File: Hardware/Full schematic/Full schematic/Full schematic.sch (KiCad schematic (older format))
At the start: 23 parts, among them J1 Conn_01x04_Male, J2 Conn_01x02_Male, U1 74LVC2T45DC, U2 74LVC2T45DC, U3 AD9835, X1 50MHz

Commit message: Fixed power control bug
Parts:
- added C10: 0.1uF, symbol Device:C
- added C11, C13: 47pF, symbol Device:C
- added C12: 56pF, symbol Device:C
- added L1, L4: 3.3uH, symbol Device:L
- added L2, L3: 4.7uH, symbol Device:L
- gave numbers to parts that had none: 6
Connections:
- net GND: now also C11.2, C12.2, C13.2
- net at R1.1, U3.14 (IOUT): now also C10.2; no longer J2.2 (Pin_2)
- new net: C10.1, L1.1
- new net: C11.1, L1.2, L2.1
- new net: J2.2 (Pin_2), L4.2
- new net: C12.1, L2.2, L3.1
- new net: C13.1, L3.2, L4.1
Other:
- note added: "Peak to peak:\n3.50MHz - ?\n3.65MHz - ?\n18.00MHz - ?\n18.25MHz - ?"
- moved on the sheet: J2
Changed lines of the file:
@@
 Wire Wire Line
 	6500 3300 6300 3300
-$Comp
-L Connector:Conn_01x02_Male J2
-U 1 1 5FE33216
-P 7050 3400
-F 0 "J2" H 7112 3444 50  0000 L CNN
-F 1 "Conn_01x02_Male" V 7203 3444 50  0000 L CNN
-F 2 "" H 7050 3400 50  0001 C CNN
-F 3 "~" H 7050 3400 50  0001 C CNN
-	1    7050 3400
-	-1   0    0    1
-$EndComp
-Wire Wire Line
-	6850 3300 6500 3300
-Connection ~ 6500 3300
-$Comp
-L power:GND #PWR026
-U 1 1 5FE3B38F
-P 6800 3450
-F 0 "#PWR026" H 6800 3200 50  0001 C CNN
-F 1 "GND" H 6805 3277 50  0000 C CNN
-F 2 "" H 6800 3450 50  0001 C CNN
-F 3 "" H 6800 3450 50  0001 C CNN
-	1    6800 3450
-	1    0    0    -1
-$EndComp
-Wire Wire Line
-	6800 3450 6800 3400
-Wire Wire Line
-	6800 3400 6850 3400
-Text Notes 7100 3350 0    50   ~ 0
-Clock out
-$Comp
-L Device:R R?
+Wire Wire Line
+	10450 3450 10450 3400
+$Comp
+L Device:R R6
 U 1 1 5FDFBB2B
 P 3800 1700
-F 0 "R?" V 3593 1700 50  0000 C CNN
+F 0 "R6" V 3593 1700 50  0000 C CNN
 F 1 "100" V 3684 1700 50  0000 C CNN
 F 2 "" V 3730 1700 50  0001 C CNN
@@
 $EndComp
 $Comp
-L Device:R R?
+L Device:R R7
 U 1 1 5FDFCB33
 P 4000 1900
-F 0 "R?" V 3793 1900 50  0000 C CNN
+F 0 "R7" V 3793 1900 50  0000 C CNN
 F 1 "100" V 3884 1900 50  0000 C CNN
 F 2 "" V 3930 1900 50  0001 C CNN
@@
 $EndComp
 $Comp
-L Device:R R?
+L Device:R R8
 U 1 1 5FDFD6DE
 P 4100 2500
-F 0 "R?" V 3893 2500 50  0000 C CNN
+F 0 "R8" V 3893 2500 50  0000 C CNN
 F 1 "100" V 3984 2500 50  0000 C CNN
 F 2 "" V 4030 2500 50  0001 C CNN
@@
 	4250 2500 5200 2500
 $Comp
-L Device:R R?
+L Device:R R3
 U 1 1 5FE1FFE2
 P 1950 1700
-F 0 "R?" V 1743 1700 50  0000 C CNN
+F 0 "R3" V 1743 1700 50  0000 C CNN
 F 1 "100" V 1950 1700 50  0000 C CNN
 F 2 "" V 1880 1700 50  0001 C CNN
@@
 $EndComp
 $Comp
-L Device:R R?
+L Device:R R4
 U 1 1 5FE20C21
 P 1950 1800
-F 0 "R?" V 1743 1800 50  0000 C CNN
+F 0 "R4" V 1743 1800 50  0000 C CNN
 F 1 "100" V 1950 1800 50  0000 C CNN
 F 2 "" V 1880 1800 50  0001 C CNN
@@
 $EndComp
 $Comp
-L Device:R R?
+L Device:R R5
 U 1 1 5FE21462
 P 1950 1900
-F 0 "R?" V 1750 1900 50  0000 C CNN
+F 0 "R5" V 1750 1900 50  0000 C CNN
 F 1 "100" V 1950 1900 50  0000 C CNN
 F 2 "" V 1880 1900 50  0001 C CNN
@@
 Wire Wire Line
 	1800 2000 2250 2000
+Text Notes 6800 3750 0    50   ~ 0
+Peak to peak:\n3.50MHz - ?\n3.65MHz - ?\n18.00MHz - ?\n18.25MHz - ?
+Wire Wire Line
+	9250 3300 10500 3300
+Text Notes 10750 3350 0    50   ~ 0
+Clock out
+Wire Wire Line
+	10450 3400 10500 3400
+$Comp
+L power:GND #PWR026
+U 1 1 5FE3B38F
+P 10450 3450
+F 0 "#PWR026" H 10450 3200 50  0001 C CNN
+F 1 "GND" H 10455 3277 50  0000 C CNN
+F 2 "" H 10450 3450 50  0001 C CNN
+F 3 "" H 10450 3450 50  0001 C CNN
+	1    10450 3450
+	1    0    0    -1
+$EndComp
+$Comp
+L Connector:Conn_01x02_Male J2
+U 1 1 5FE33216
+P 10700 3400
+F 0 "J2" H 10762 3444 50  0000 L CNN
+F 1 "Conn_01x02_Male" V 10853 3444 50  0000 L CNN
+F 2 "" H 10700 3400 50  0001 C CNN
+F 3 "~" H 10700 3400 50  0001 C CNN
+	1    10700 3400
+	-1   0    0    1
+$EndComp
+$Comp
+L Device:L L1
+U 1 1 5FE327AF
+P 7900 3300
+F 0 "L1" V 8090 3300 50  0000 C CNN
+F 1 "3.3uH" V 7999 3300 50  0000 C CNN
+F 2 "" H 7900 3300 50  0001 C CNN
+F 3 "~" H 7900 3300 50  0001 C CNN
+	1    7900 3300
+	0    -1   -1   0
+$EndComp
+$Comp
+L Device:L L2
+U 1 1 5FE336B0
+P 8300 3300
+F 0 "L2" V 8490 3300 50  0000 C CNN
+F 1 "4.7uH" V 8399 3300 50  0000 C CNN
+F 2 "" H 8300 3300 50  0001 C CNN
+F 3 "~" H 8300 3300 50  0001 C CNN
+	1    8300 3300
+	0    -1   -1   0
+$EndComp
+$Comp
+L Device:L L3
+U 1 1 5FE34313
+P 8700 3300
+F 0 "L3" V 8890 3300 50  0000 C CNN
+F 1 "4.7uH" V 8799 3300 50  0000 C CNN
+F 2 "" H 8700 3300 50  0001 C CNN
+F 3 "~" H 8700 3300 50  0001 C CNN
+	1    8700 3300
+	0    -1   -1   0
+$EndComp
+$Comp
+L Device:L L4
+U 1 1 5FE38CF5
+P 9100 3300
+F 0 "L4" V 9290 3300 50  0000 C CNN
+F 1 "3.3uH" V 9199 3300 50  0000 C CNN
+F 2 "" H 9100 3300 50  0001 C CNN
+F 3 "~" H 9100 3300 50  0001 C CNN
+	1    9100 3300
+	0    -1   -1   0
+$EndComp
+$Comp
+L Device:C C10
+U 1 1 5FE39BF1
+P 7550 3300
+F 0 "C10" V 7298 3300 50  0000 C CNN
+F 1 "0.1uF" V 7389 3300 50  0000 C CNN
+F 2 "" H 7588 3150 50  0001 C CNN
+F 3 "~" H 7550 3300 50  0001 C CNN
+	1    7550 3300
+	0    1    1    0
+$EndComp
+$Comp
+L Device:C C11
+U 1 1 5FE3AC6F
+P 8100 3500
+F 0 "C11" H 8215 3546 50  0000 L CNN
+F 1 "47pF" H 8215 3455 50  0000 L CNN
+F 2 "" H 8138 3350 50  0001 C CNN
+F 3 "~" H 8100 3500 50  0001 C CNN
+	1    8100 3500
+	1    0    0    -1
+$EndComp
+$Comp
+L Device:C C12
+U 1 1 5FE3B796
+P 8500 3500
+F 0 "C12" H 8615 3546 50  0000 L CNN
+F 1 "56pF" H 8615 3455 50  0000 L CNN
+F 2 "" H 8538 3350 50  0001 C CNN
+F 3 "~" H 8500 3500 50  0001 C CNN
+	1    8500 3500
+	1    0    0    -1
+$EndComp
+$Comp
+L Device:C C13
+U 1 1 5FE3C0D8
+P 8900 3500
+F 0 "C13" H 9015 3546 50  0000 L CNN
+F 1 "47pF" H 9015 3455 50  0000 L CNN
+F 2 "" H 8938 3350 50  0001 C CNN
+F 3 "~" H 8900 3500 50  0001 C CNN
+	1    8900 3500
+	1    0    0    -1
+$EndComp
+$Comp
+L power:GND #PWR028
+U 1 1 5FE3D0F2
+P 8100 3700
+F 0 "#PWR028" H 8100 3450 50  0001 C CNN
+F 1 "GND" H 8105 3527 50  0000 C CNN
+F 2 "" H 8100 3700 50  0001 C CNN
+F 3 "" H 8100 3700 50  0001 C CNN
+	1    8100 3700
+	1    0    0    -1
+$EndComp
+$Comp
+L power:GND #PWR029
+U 1 1 5FE3DCD9
+P 8500 3700
+F 0 "#PWR029" H 8500 3450 50  0001 C CNN
+F 1 "GND" H 8505 3527 50  0000 C CNN
+F 2 "" H 8500 3700 50  0001 C CNN
+F 3 "" H 8500 3700 50  0001 C CNN
+	1    8500 3700
+	1    0    0    -1
+$EndComp
+$Comp
+L power:GND #PWR030
+U 1 1 5FE3E756
+P 8900 3700
+F 0 "#PWR030" H 8900 3450 50  0001 C CNN
+F 1 "GND" H 8905 3527 50  0000 C CNN
+F 2 "" H 8900 3700 50  0001 C CNN
+F 3 "" H 8900 3700 50  0001 C CNN
+	1    8900 3700
+	1    0    0    -1
+$EndComp
+Wire Wire Line
+	7400 3300 6500 3300
+Connection ~ 6500 3300
+Wire Wire Line
+	8050 3300 8100 3300
+Wire Wire Line
+	8100 3350 8100 3300
+Connection ~ 8100 3300
+Wire Wire Line
+	8100 3300 8150 3300
+Wire Wire Line
+	8450 3300 8500 3300
+Wire Wire Line
+	8500 3350 8500 3300
+Connection ~ 8500 3300
+Wire Wire Line
+	8500 3300 8550 3300
+Wire Wire Line
+	8850 3300 8900 3300
+Wire Wire Line
+	8900 3350 8900 3300
+Connection ~ 8900 3300
+Wire Wire Line
+	8900 3300 8950 3300
+Wire Wire Line
+	8100 3700 8100 3650
+Wire Wire Line
+	7750 3300 7700 3300
+Wire Wire Line
+	8500 3700 8500 3650
+Wire Wire Line
+	8900 3700 8900 3650
 $EndSCHEMATC

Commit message: Working 3.5MHz tract.
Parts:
- added C14, C15, C16, C21: 0.1uF, symbol Device:C
- added C17: 100pF, symbol Device:C
- added C18, C22, C23, C24, C25: C, symbol Device:C
- added C19: 1nF, symbol Device:C
- added C20: 1000uF x 25V, symbol Device:CP
- added DA1: AD825, symbol Fossa_library:AD825
- added J3, J4, J5: Conn_01x02_Male, symbol Connector:Conn_01x02_Male
- added L5: 2.2uH, symbol Device:L
- added L6: 5uH, symbol Device:L
- added Q1: IRF610, symbol Device:Q_NMOS_GDS
- added Q2: BSS138, Package_TO_SOT_SMD:SOT-23, symbol Transistor_FET:BSS138
- added R10: 2k, symbol Device:R
- added R11, R9: 4.7k, symbol Device:R
- added R12: 15k, symbol Device:R
- added R13: 10k, symbol Device:R
- added R14: 100, symbol Device:R
- added RV1: 5k, symbol Device:R_POT
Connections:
- net GND: now also C15.2, C16.2, C17.2, C19.2, C20.2, C24.1, DA1.4 (-VS), J3.2 (Pin_2), J4.1 (Pin_1), J5.1 (Pin_1), Q1.3 (S), Q2.2 (S), R10.2, R9.2
- net at J2.2 (Pin_2), L4.2: now also C14.2, R9.1
- new net: C14.1, R11.2
- new net: DA1.2 (-IN), R11.1, R12.2
- new net: DA1.3 (+IN), RV1.2
- new net: DA1.6 (OUT), Q1.1 (G), R12.1
- new net: C16.1, C20.1, J4.2 (Pin_2), L5.1
- new net: C21.2, L5.2, Q1.2 (D)
- new net: C17.1, C21.1, L6.1
- new net: C18.1, J5.2 (Pin_2), L6.2
- new net: C18.2, C22.1
- new net: C22.2, C23.1
- new net: C23.2, C25.2
- new net: C24.2, C25.1
- new net: R10.1, RV1.1
- new net: Q2.3 (D), R13.1, RV1.3
- new net: C19.1, Q2.1 (G), R14.1
- new net: J3.1 (Pin_1), R14.2
- new net +12V: C15.1, DA1.7 (+VS), R13.2
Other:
- note added: "290pF"
- note added: "Manipulation\n1 - OFF\n0 - ON"
- note added: "Output stage power"
- note added: "Peak to peak (IN):\n3.50MHz - 0.34V\n3.65MHz - 0.3V\n18.00MHz - 1.5V\n18.25MHz - 1V"
- note added: "Peak to peak (out):\n3.50MHz - 1V\n3.65MHz - 0.96V\n18.00MHz - 0.8V\n18.25MHz - 0.7V"
- note added: "To ICS501 - 144MHz tract"
- note added: "To antenna"
- note removed: "Clock out"
- note removed: "Peak to peak:\n3.50MHz - ?\n3.65MHz - ?\n18.00MHz - ?\n18.25MHz - ?"
- moved on the sheet: C10, C11, C12, C13, L1, L2, L3, L4

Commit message: Added amplitude at antenna detector
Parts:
- added C21: 0.01uF, symbol Device:C
- added D1: 1N4148W, Diode_SMD:D_SOD-123, symbol Diode:1N4148W
- added D2: 1N4728A, Diode_THT:D_DO-41_SOD81_P10.16mm_Horizontal, symbol Diode:1N47xxA
- added J5: Conn_01x02_Male, symbol Connector:Conn_01x02_Male
- added R15: 220k, symbol Device:R
- added R16: 11k, symbol Device:R
- added R17: 39k, symbol Device:R
- added R18: 10k, symbol Device:R
- renumbered C19 to C15, C15 to C16, C20 to C17, C16 to C18, C21 to C19, C17 to C20, C18 to C22, C22 to C23, C23 to C24, C24 to C25, C25 to C26, J5 to J6, Q2 to Q1, Q1 to Q2, R3 to R1, R14 to R12, R12 to R13, R13 to R14, R4 to R2, R5 to R3, R6 to R4, R7 to R5, R8 to R6, R1 to R7, R2 to R8
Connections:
- net GND: now also C21.2, D2.2 (A), J5.1 (Pin_1), R16.2, R18.2
- net ANT_3.5: now reaches C22.1, J6.2 (Pin_2), L6.2
- net ANT_3.5: now also R15.1
- new net: D1.2 (A), R15.2, R16.1
- new net: C21.1, D1.1 (K), R17.2
- new net: D2.1 (K), J5.2 (Pin_2), R17.1, R18.1
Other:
- note added: "0.00972*Uant"
- note added: "200V P-P at antenna equivalent.\nAntenna equivalent is 240 Ohm resistor\nin series with 35pF capacitor."
- note added: "Peak to peak (in):\n3.50MHz - 0.34V\n3.65MHz - 0.3V\n18.00MHz - 1.5V\n18.25MHz - 1V"
- note added: "To ADC"
- note removed: "Peak to peak (IN):\n3.50MHz - 0.34V\n3.65MHz - 0.3V\n18.00MHz - 1.5V\n18.25MHz - 1V"

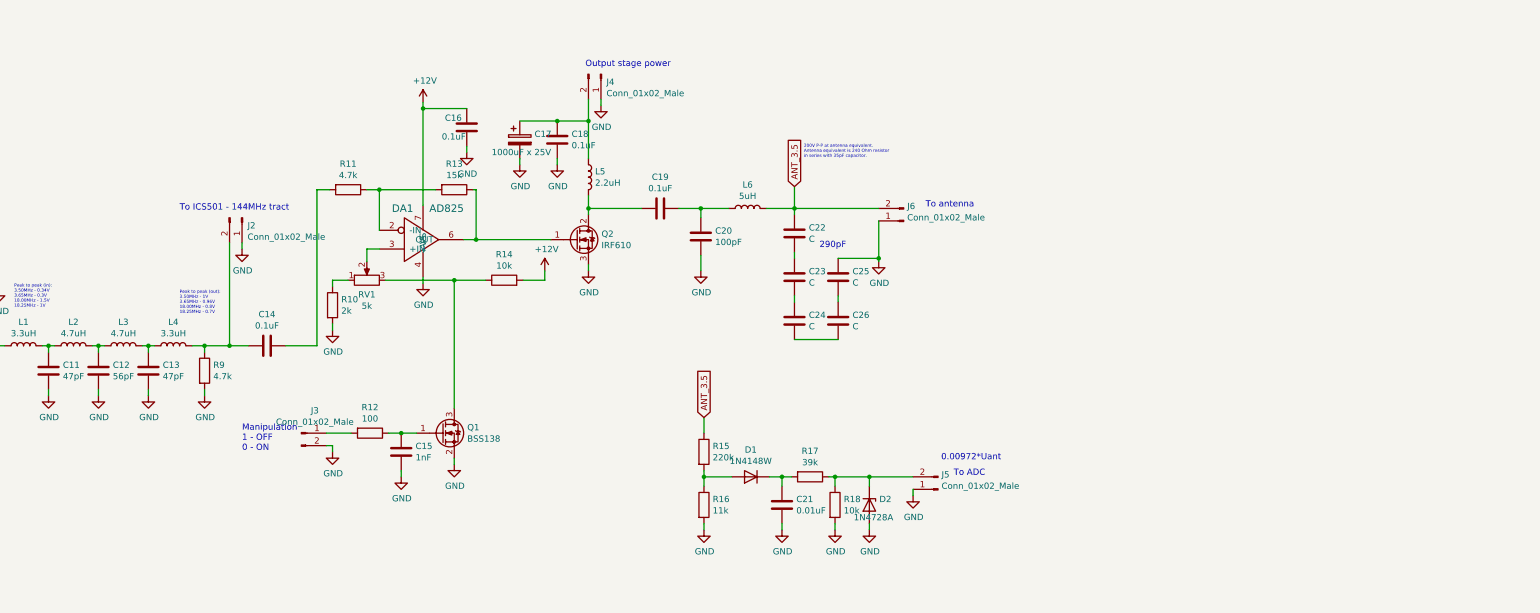
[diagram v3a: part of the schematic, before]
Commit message: Added antenna matching, ready to draw PCB
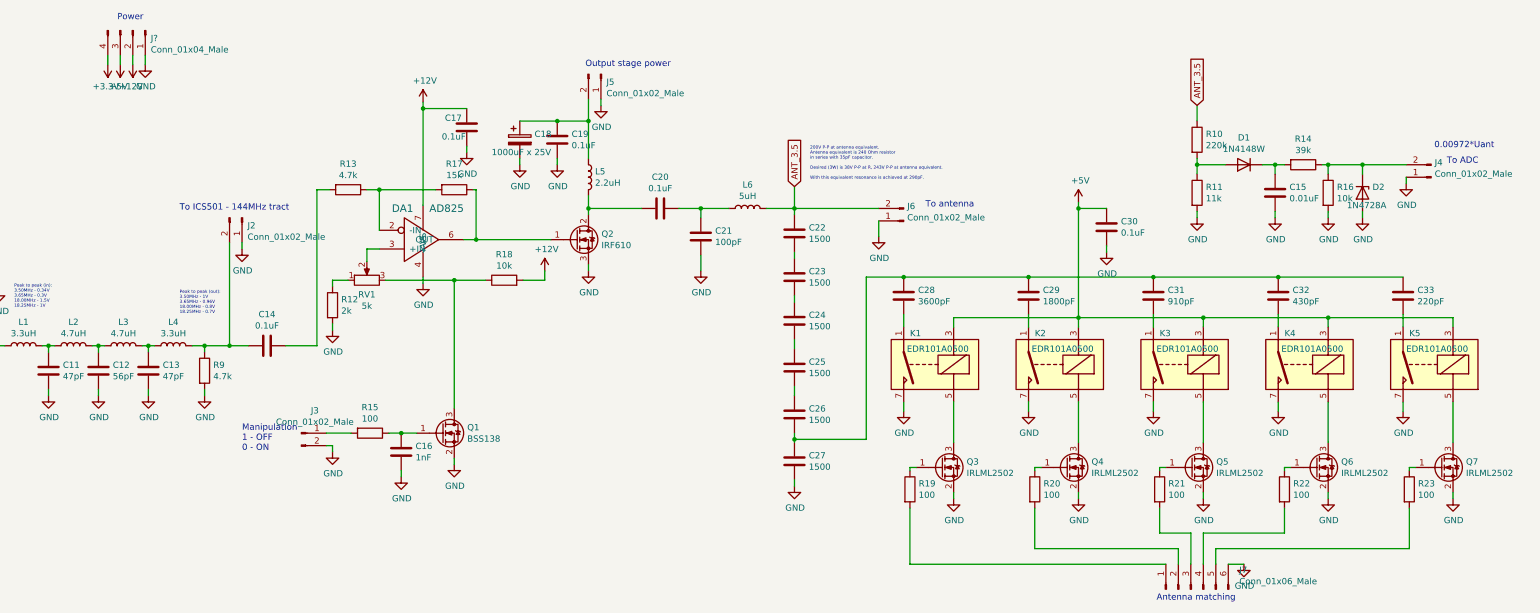
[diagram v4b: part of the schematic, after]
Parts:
- added C27: 1500, symbol Device:C
- added C28: 3600pF, symbol Device:C
- added C29: 1800pF, symbol Device:C
- added C30: 0.1uF, symbol Device:C
- added C31: 910pF, symbol Device:C
- added C32: 430pF, symbol Device:C
- added C33: 220pF, symbol Device:C
- added J7: Conn_01x06_Male, symbol Connector:Conn_01x06_Male
- added J?: Conn_01x04_Male, symbol Connector:Conn_01x04_Male
- added K1, K2, K3, K4, K5: EDR101A0500, Relay_THT:Relay_SPST_StandexMeder_MS_Form1AB, symbol Fossa_library:EDR101A0500
- added Q3, Q4, Q5, Q6, Q7: IRLML2502, symbol Device:Q_NMOS_GSD
- added R19, R20, R21, R22, R23: 100, symbol Device:R
- C22, C23, C24, C25, C26: value C -> 1500
- renumbered C21 to C15, C15 to C16, C16 to C17, C17 to C18, C18 to C19, C19 to C20, C20 to C21, J5 to J4, J4 to J5, R15 to R10, R16 to R11, R10 to R12, R11 to R13, R17 to R14, R12 to R15, R18 to R16, R13 to R17, R14 to R18
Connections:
- net +12V: now also J?.2 (Pin_2)
- net +3V3: now also J?.4 (Pin_4)
- net +5V: now also C30.1, J?.3 (Pin_3), K1.3, K2.3, K3.3, K4.3, K5.3
- net GND: now also C27.2, C30.2, J7.6 (Pin_6), J?.1 (Pin_1), K1.7, K2.7, K3.7, K4.7, K5.7, Q3.2 (S), Q4.2 (S), Q5.2 (S), Q6.2 (S), Q7.2 (S); no longer C25.1
- net at C24.2: now also C25.1; no longer C26.2
- new net: C26.2, C27.1, C28.1, C29.1, C31.1, C32.1, C33.1
- new net: C28.2, K1.1
- new net: K1.5, Q3.3 (D)
- new net: C29.2, K2.1
- new net: K2.5, Q4.3 (D)
- new net: C31.2, K3.1
- new net: K3.5, Q5.3 (D)
- new net: C32.2, K4.1
- new net: K4.5, Q6.3 (D)
- new net: C33.2, K5.1
- new net: K5.5, Q7.3 (D)
- new net: Q3.1 (G), R19.1
- new net: J7.1 (Pin_1), R19.2
- new net: Q4.1 (G), R20.1
- new net: J7.2 (Pin_2), R20.2
- new net: Q5.1 (G), R21.1
- new net: J7.3 (Pin_3), R21.2
- new net: Q6.1 (G), R22.1
- new net: J7.4 (Pin_4), R22.2
- new net: Q7.1 (G), R23.1
- new net: J7.5 (Pin_5), R23.2
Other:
- note added: "200V P-P at antenna equivalent.\nAntenna equivalent is 240 Ohm resistor\nin series with 35pF capacitor.\n\nDesired (3W) is 38V P-P at R, 243V P-P at antenna equivalent.\n\nWith this equivalent resonance is achieved at 290pF."
- note added: "Antenna matching"
- note added: "Power"
- note removed: "200V P-P at antenna equivalent.\nAntenna equivalent is 240 Ohm resistor\nin series with 35pF capacitor."
- note removed: "290pF"
- moved on the sheet: C15, C25, C26, D1, D2, J4, R10, R11, R14, R16

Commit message: PCB is ready
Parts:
- removed C16: 1nF, symbol Device:C
- removed C22, C23: 1500, symbol Device:C
- removed R17: 15k, symbol Device:R
- removed R18: 10k, symbol Device:R
- removed X1: 50MHz, Oscillator:Oscillator_SMD_EuroQuartz_XO32-4Pin_3.2x2.5mm, symbol Oscillator:XO32
- added C10: 470uF x 6V, Capacitor_THT:CP_Radial_D10.0mm_P5.00mm, symbol Device:CP
- added C12: 470uF x 10V, Capacitor_THT:CP_Radial_D10.0mm_P5.00mm, symbol Device:CP
- added C14: 470uF x 16V, Capacitor_THT:CP_Radial_D10.0mm_P5.00mm, symbol Device:CP
- added C30, C34, C35: 200pF, Capacitor_SMD:C_0805_2012Metric_Pad1.18x1.45mm_HandSolder, symbol Device:C
- added C37, C38, C39, C40, C41, C42: 100pF, Capacitor_SMD:C_0805_2012Metric_Pad1.18x1.45mm_HandSolder, symbol Device:C
- added C43, C44, C45, C46, C47, C48: 47pF, Capacitor_SMD:C_0805_2012Metric_Pad1.18x1.45mm_HandSolder, symbol Device:C
- added C49, C50, C51, C52, C53, C54: 24pF, Capacitor_SMD:C_0805_2012Metric_Pad1.18x1.45mm_HandSolder, symbol Device:C
- added C55: 10nF, Capacitor_SMD:C_0805_2012Metric_Pad1.18x1.45mm_HandSolder, symbol Device:C
- added R11: 56k, Resistor_SMD:R_0805_2012Metric_Pad1.20x1.40mm_HandSolder, symbol Device:R
- added X1: 50MHz, Oscillator:Oscillator_DIP-8, symbol Oscillator:CXO_DIP8
- C1, C2, C3, C4, C5, C6, C7, C8, C9: footprint (none) -> Capacitor_SMD:C_0805_2012Metric_Pad1.18x1.45mm_HandSolder
- C11: renamed from C10; footprint (none) -> Capacitor_SMD:C_0805_2012Metric_Pad1.18x1.45mm_HandSolder
- C13: renamed from C11; footprint (none) -> Capacitor_SMD:C_0805_2012Metric_Pad1.18x1.45mm_HandSolder
- C15: renamed from C12; footprint (none) -> Capacitor_SMD:C_0805_2012Metric_Pad1.18x1.45mm_HandSolder
- C16: renamed from C13; footprint (none) -> Capacitor_SMD:C_0805_2012Metric_Pad1.18x1.45mm_HandSolder
- C17: renamed from C14; footprint (none) -> Capacitor_SMD:C_0805_2012Metric_Pad1.18x1.45mm_HandSolder
- C18: renamed from C17; footprint (none) -> Capacitor_SMD:C_0805_2012Metric_Pad1.18x1.45mm_HandSolder
- C19: renamed from C18; footprint (none) -> Capacitor_THT:CP_Radial_D14.0mm_P7.50mm
- C20: renamed from C19; footprint (none) -> Capacitor_SMD:C_0805_2012Metric_Pad1.18x1.45mm_HandSolder
- C21: renamed from C20; footprint (none) -> Capacitor_SMD:C_0805_2012Metric_Pad1.18x1.45mm_HandSolder
- C22: renamed from C21; value 100pF -> 75pF; footprint (none) -> Capacitor_SMD:C_0805_2012Metric_Pad1.18x1.45mm_HandSolder
- C23: renamed from C15; footprint (none) -> Capacitor_SMD:C_0805_2012Metric_Pad1.18x1.45mm_HandSolder
- C24, C25, C26, C27: value 1500 -> 390pF; footprint (none) -> Capacitor_SMD:C_0805_2012Metric_Pad1.18x1.45mm_HandSolder
- C28: value 3600pF -> 390pF; footprint (none) -> Capacitor_SMD:C_0805_2012Metric_Pad1.18x1.45mm_HandSolder
- C29: value 1800pF -> 390pF; footprint (none) -> Capacitor_SMD:C_0805_2012Metric_Pad1.18x1.45mm_HandSolder
- C31: value 910pF -> 200pF; footprint (none) -> Capacitor_SMD:C_0805_2012Metric_Pad1.18x1.45mm_HandSolder
- C32: value 430pF -> 200pF; footprint (none) -> Capacitor_SMD:C_0805_2012Metric_Pad1.18x1.45mm_HandSolder
- C33: value 220pF -> 200pF; footprint (none) -> Capacitor_SMD:C_0805_2012Metric_Pad1.18x1.45mm_HandSolder
- C36: renamed from C30; footprint (none) -> Capacitor_SMD:C_0805_2012Metric_Pad1.18x1.45mm_HandSolder
- DA1: footprint (none) -> Package_SO:SOIC-8_3.9x4.9mm_P1.27mm
- J1: footprint (none) -> Connector_PinHeader_2.54mm:PinHeader_1x04_P2.54mm_Vertical
- J2: renamed from J?; footprint (none) -> Connector_PinHeader_2.54mm:PinHeader_1x04_P2.54mm_Vertical
- J3: renamed from J2; footprint (none) -> Connector_PinHeader_2.54mm:PinHeader_1x02_P2.54mm_Vertical
- J4: renamed from J3; footprint (none) -> Connector_PinHeader_2.54mm:PinHeader_1x02_P2.54mm_Vertical
- J5: footprint (none) -> Connector_PinHeader_2.54mm:PinHeader_1x02_P2.54mm_Vertical
- J6: renamed from J4; footprint (none) -> Connector_PinHeader_2.54mm:PinHeader_1x02_P2.54mm_Vertical
- J7: renamed from J6; footprint (none) -> Connector_PinHeader_2.54mm:PinHeader_1x02_P2.54mm_Vertical
- J8: renamed from J7; footprint (none) -> Connector_PinHeader_2.54mm:PinHeader_1x06_P2.54mm_Vertical
- L1, L2, L3, L4: footprint (none) -> Inductor_THT:L_Radial_D9.5mm_P5.00mm_Fastron_07HVP
- L5: value 2.2uH -> 10uH; footprint (none) -> Inductor_THT:L_Radial_D9.5mm_P5.00mm_Fastron_07HVP
- L6: value 5uH -> 21uH; footprint (none) -> Inductor_THT:L_Radial_D9.5mm_P5.00mm_Fastron_07HVP
- Q2: footprint (none) -> Package_TO_SOT_THT:TO-220-3_Horizontal_TabDown
- Q3, Q4, Q5, Q6, Q7: footprint (none) -> Package_TO_SOT_SMD:SOT-23
- R1, R2, R3, R4, R5, R6, R7, R8, R9: footprint (none) -> Resistor_SMD:R_0805_2012Metric_Pad1.20x1.40mm_HandSolder
- R10: renamed from R15; footprint (none) -> Resistor_SMD:R_0805_2012Metric_Pad1.20x1.40mm_HandSolder
- R12: value 2k -> 3.9k; footprint (none) -> Resistor_SMD:R_0805_2012Metric_Pad1.20x1.40mm_HandSolder
- R13: value 4.7k -> 2k; footprint (none) -> Resistor_SMD:R_0805_2012Metric_Pad1.20x1.40mm_HandSolder
- R14: renamed from R10; footprint (none) -> Resistor_SMD:R_0805_2012Metric_Pad1.20x1.40mm_HandSolder
- R15: renamed from R11; footprint (none) -> Resistor_SMD:R_0805_2012Metric_Pad1.20x1.40mm_HandSolder
- R16: renamed from R14; footprint (none) -> Resistor_SMD:R_0805_2012Metric_Pad1.20x1.40mm_HandSolder
- R17: renamed from R16; footprint (none) -> Resistor_SMD:R_0805_2012Metric_Pad1.20x1.40mm_HandSolder
- R18: renamed from R19; footprint (none) -> Resistor_SMD:R_0805_2012Metric_Pad1.20x1.40mm_HandSolder
- R19: renamed from R20; footprint (none) -> Resistor_SMD:R_0805_2012Metric_Pad1.20x1.40mm_HandSolder
- R20: renamed from R21; footprint (none) -> Resistor_SMD:R_0805_2012Metric_Pad1.20x1.40mm_HandSolder
- R21: renamed from R22; footprint (none) -> Resistor_SMD:R_0805_2012Metric_Pad1.20x1.40mm_HandSolder
- R22: renamed from R23; footprint (none) -> Resistor_SMD:R_0805_2012Metric_Pad1.20x1.40mm_HandSolder
- RV1: value 5k -> 20k; footprint (none) -> Potentiometer_THT:Potentiometer_Bourns_3386C_Horizontal
- U3: footprint (none) -> Package_SO:SSOP-16_4.4x5.2mm_P0.65mm
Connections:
- net +12V: now also C14.1, R11.1
- net +3V3: now also C10.1
- net +5V: now also C12.1, X1.8 (Vcc)
- net ANT_3.5: now also C24.1, C30.1, C37.1, C43.1, C49.1
- net GND: now also R13.2, RV1.1, C10.2, C12.2, C14.2, C55.2, X1.4 (GND); no longer C27.2, R12.2
- net at U3.6 (MCLK): now also X1.5 (OUT)
- net at C17.1: now also DA1.3 (+IN), RV1.2; no longer R13.2
- net at DA1.2 (-IN), R13.1: now also R12.2
- net at DA1.6 (OUT), Q2.1 (G): now also R12.1
- net at Q1.3 (D), RV1.3: now also C55.1, R11.2
- net at K1.1: now also C29.2; no longer C28.2
- net at K2.1: now also C35.2; no longer C29.2
- net at K3.1: now also C42.2; no longer C31.2
- net at K4.1: now also C48.2; no longer C32.2
- net at K5.1: now also C54.2; no longer C33.2
- new net: C28.2, C29.1
- new net: C27.2, C28.1
- new net: C26.2, C27.1
- new net: C34.2, C35.1
- new net: C33.2, C34.1
- new net: C32.2, C33.1
- new net: C31.2, C32.1
- new net: C30.2, C31.1
- new net: C41.2, C42.1
- new net: C40.2, C41.1
- new net: C39.2, C40.1
- new net: C38.2, C39.1
- new net: C37.2, C38.1
- new net: C47.2, C48.1
- new net: C46.2, C47.1
- new net: C45.2, C46.1
- new net: C44.2, C45.1
- new net: C43.2, C44.1
- new net: C53.2, C54.1
- new net: C52.2, C53.1
- new net: C51.2, C52.1
- new net: C50.2, C51.1
- new net: C49.2, C50.1
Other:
- note added: "16pF"
- note added: "200V P-P at antenna equivalent.\nAntenna equivalent is 240 Ohm resistor\nin series with 35pF capacitor.\n\nDesired (3W) is 38V P-P at R, 243V P-P at antenna equivalent.\n\nWith this equivalent resonance is achieved at 70pF."
- note added: "32pF"
- note added: "4pF"
- note added: "64pF"
- note added: "8pF"
- note removed: "200V P-P at antenna equivalent.\nAntenna equivalent is 240 Ohm resistor\nin series with 35pF capacitor.\n\nDesired (3W) is 38V P-P at R, 243V P-P at antenna equivalent.\n\nWith this equivalent resonance is achieved at 290pF."
- moved on the sheet: C23, C36, D1, D2, DA1, J4, J6, J8, K1, K2, K3, K4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
